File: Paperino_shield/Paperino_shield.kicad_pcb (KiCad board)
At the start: 2 copper layers, 67.3 x 36.9 mm, 6 parts, among them M1 Mounting_hole, M2 Mounting_hole, M3 Mounting_hole, M4 Mounting_hole

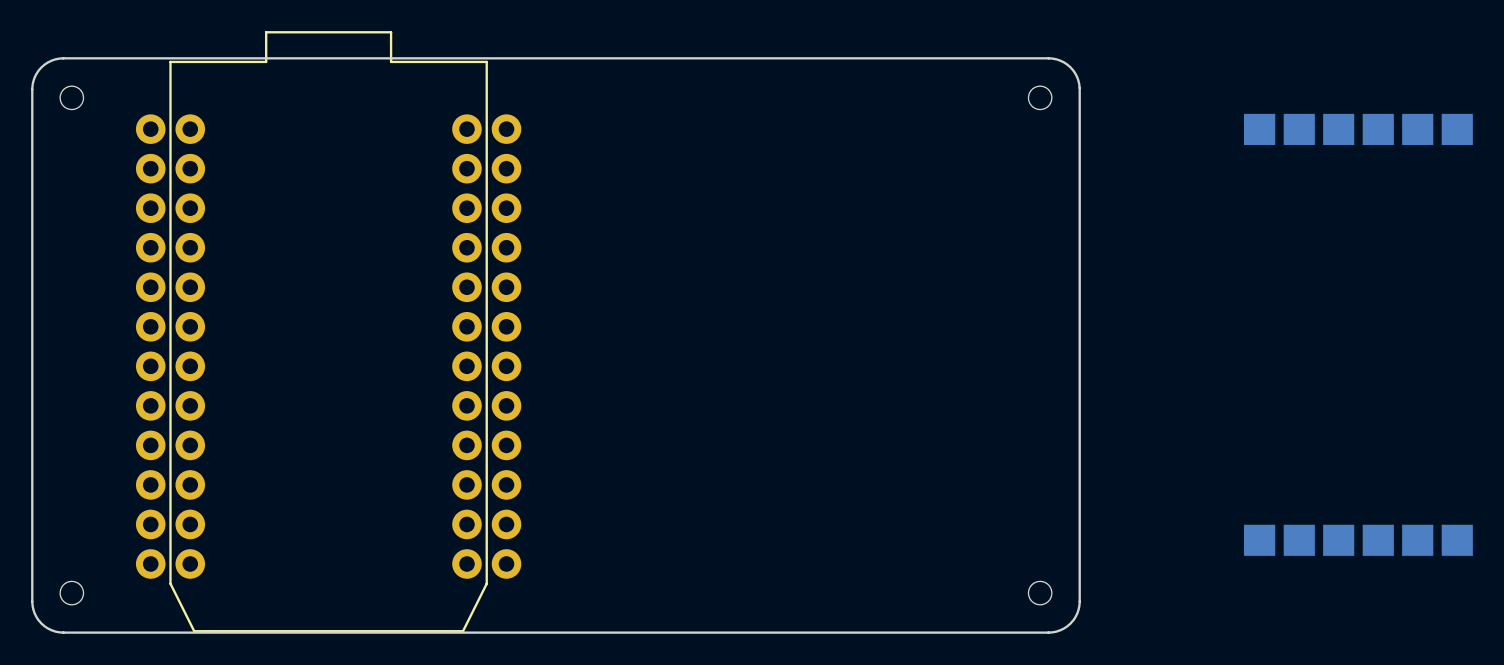
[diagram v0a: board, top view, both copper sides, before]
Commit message: shield mechanical layers
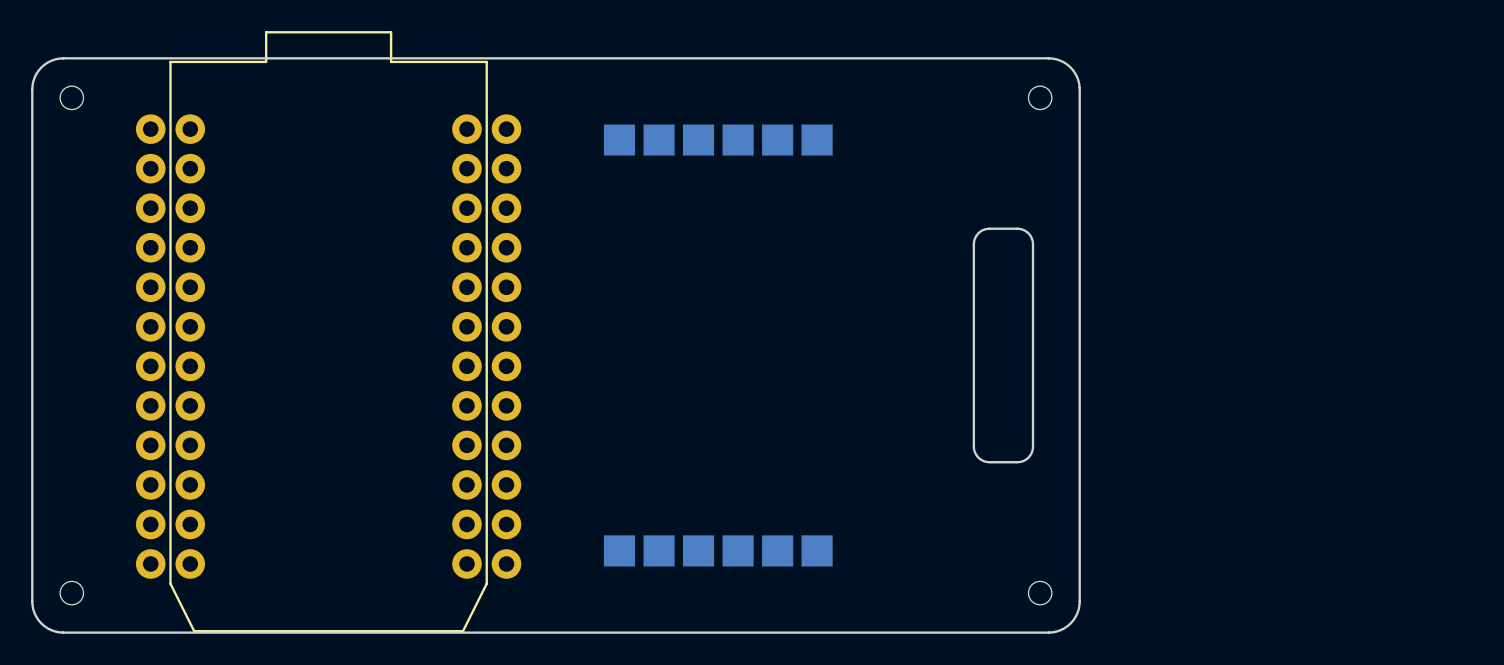
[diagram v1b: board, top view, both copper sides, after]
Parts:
- moved A2 41.1 mm to (147.0, 81.5)
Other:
- outline, holes or cut-outs redrawn
- board text added: "z-axis milling top side -0.8 mm"
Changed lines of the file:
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@@
     (area 99.924999 63.024999 167.375001 100.075001)
     (thickness 1.6)
-    (drawings 8)
+    (drawings 29)
     (tracks 0)
     (zones 0)
@@
     (zone_45_only no)
     (trace_min 0.2)
-    (segment_width 0.2)
+    (segment_width 0.15)
     (edge_width 0.15)
     (via_size 0.6)
@@
     (aux_axis_origin 0 0)
     (grid_origin 100 100)
-    (visible_elements FFFFFF7F)
+    (visible_elements 7FFFFFFF)
     (pcbplotparams
       (layerselection 0x00030_80000001)
@@
       (net 23 +3V3))
   )
-  (module Paperino:paperino_module (layer B.Cu)
-    (at 188.16 80.87 90)
+  (module Paperino:paperino_module locked (layer B.Cu)
+    (at 147.03 81.55 90)
     (fp_text reference A2 (at -11.1 12.35 90) (layer B.SilkS) hide
       (effects (font (size 1 1) (thickness 0.15)) (justify mirror))
@@
     (pad "" np_thru_hole circle (at 0 0) (size 1.5 1.5) (drill 1.5) (layers *.Cu *.Mask))
   )
+  (gr_text "z-axis milling\ntop side\n-0.8 mm" (at 146.91 81.89) (layer Eco1.User)
+    (effects (font (size 1.5 1.5) (thickness 0.3)))
+  )
+  (gr_line (start 132.7 67.27) (end 132.7 95.83) (layer Eco1.User) (width 0.15))
+  (gr_arc (start 133.7 67.27) (end 132.7 67.27) (angle 90) (layer Eco1.User) (width 0.15))
+  (gr_line (start 155.22 66.27) (end 133.7 66.27) (layer Eco1.User) (width 0.15))
+  (gr_arc (start 155.22 67.27) (end 155.22 66.27) (angle 90) (layer Eco1.User) (width 0.15))
+  (gr_line (start 156.22 74.05) (end 156.22 67.27) (layer Eco1.User) (width 0.15))
+  (gr_line (start 162 74.05) (end 156.22 74.05) (layer Eco1.User) (width 0.15))
+  (gr_arc (start 133.7 95.83) (end 133.7 96.83) (angle 90) (layer Eco1.User) (width 0.15))
+  (gr_line (start 155.22 96.83) (end 133.7 96.83) (layer Eco1.User) (width 0.15))
+  (gr_arc (start 155.22 95.83) (end 156.22 95.83) (angle 90) (layer Eco1.User) (width 0.15))
+  (gr_line (start 156.22 89.05) (end 156.22 95.83) (layer Eco1.User) (width 0.15))
+  (gr_line (start 162 89.05) (end 156.22 89.05) (layer Eco1.User) (width 0.15))
+  (gr_line (start 162 89.05) (end 162 74.05) (layer Eco1.User) (width 0.15))
+  (gr_arc (start 161.5 75.05) (end 161.5 74.05) (angle -90) (layer Edge.Cuts) (width 0.15))
+  (gr_line (start 160.5 75.05) (end 160.5 88.05) (layer Edge.Cuts) (width 0.15))
+  (gr_arc (start 161.5 88.05) (end 161.5 89.05) (angle 90) (layer Edge.Cuts) (width 0.15))
+  (gr_line (start 163.3 89.05) (end 161.5 89.05) (layer Edge.Cuts) (width 0.15))
+  (gr_line (start 163.3 74.05) (end 161.5 74.05) (layer Edge.Cuts) (width 0.15))
+  (gr_arc (start 163.3 75.05) (end 163.3 74.05) (angle 90) (layer Edge.Cuts) (width 0.15))
+  (gr_arc (start 163.3 88.05) (end 164.3 88.05) (angle 90) (layer Edge.Cuts) (width 0.15))
+  (gr_line (start 164.3 75.05) (end 164.3 88.05) (layer Edge.Cuts) (width 0.15))
   (gr_arc (start 165.3 65.1) (end 165.3 63.1) (angle 87.13759477) (layer Edge.Cuts) (width 0.15))
   (gr_arc (start 165.3 98) (end 167.3 98) (angle 90) (layer Edge.Cuts) (width 0.15))

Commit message: shield: preliminary layout done
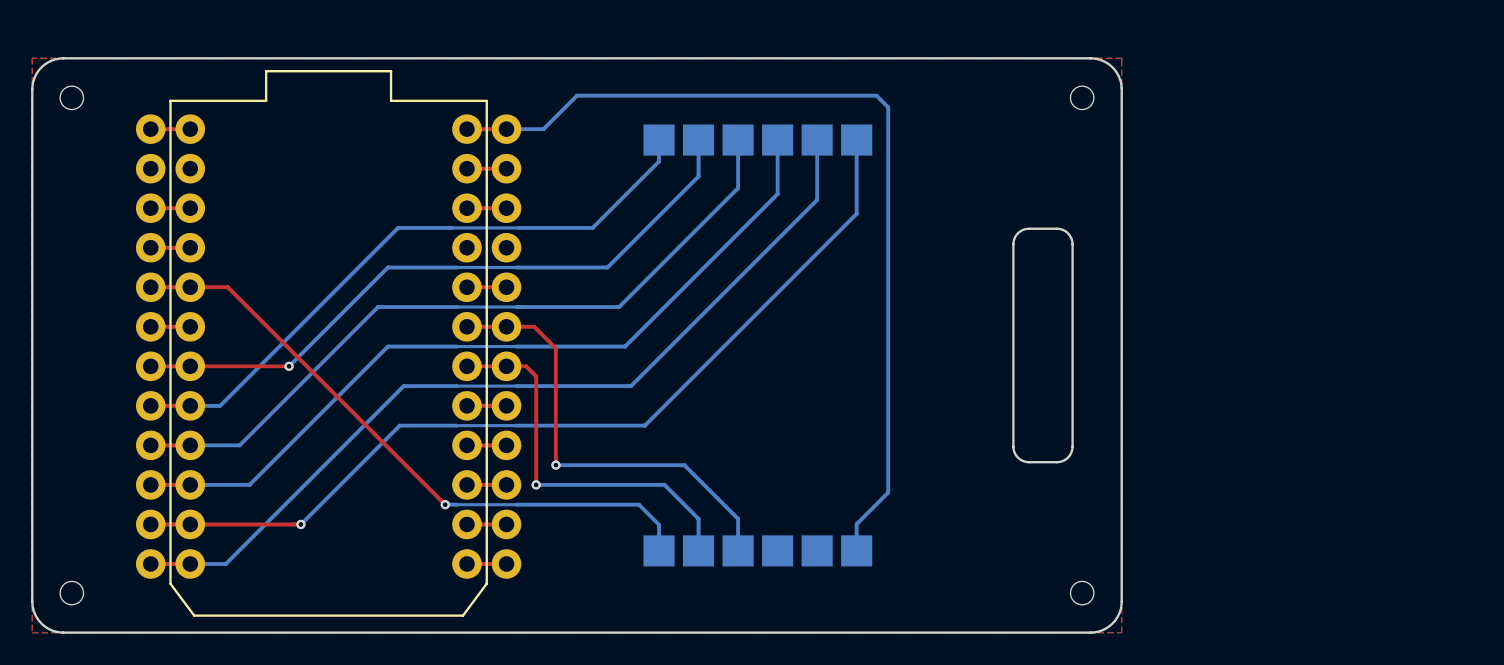
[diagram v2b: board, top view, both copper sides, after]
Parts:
- moved M2 2.70 mm to (167.5, 65.6)
- moved M4 2.70 mm to (167.5, 97.5)
- moved A2 2.54 mm to (149.6, 81.5)
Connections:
- A1 pad 18: Net-(A1-Pad18) -> /INT2
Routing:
- net /~BUSY: track 0.00 -> 57.9 mm, vias 0 -> 1
- net +3V3: track 0.00 -> 57.1 mm
- net /~RST: track 0.00 -> 55.9 mm
- net /SPI_CS1: track 0.00 -> 51.0 mm
- net /SPI_CLK: track 0.00 -> 47.4 mm
- net /SPI_MOSI: track 0.00 -> 42.1 mm, vias 0 -> 1
- net /INT1: track 0.00 -> 40.2 mm, vias 0 -> 1
- net /SPI_MISO: track 0.00 -> 40.0 mm
- net /SPI_CS2: track 0.00 -> 28.5 mm, vias 0 -> 1
- net /INT2: track 0.00 -> 24.6 mm, vias 0 -> 1
- net Net-(A1-Pad6): track 0.00 -> 2.54 mm
- net Net-(A1-Pad4): track 0.00 -> 2.54 mm
- net Net-(A1-Pad3): track 0.00 -> 2.54 mm
- net Net-(A1-Pad1): track 0.00 -> 2.54 mm
- net Net-(A1-Pad23): track 0.00 -> 2.54 mm
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- added copper zone on B.Cu, net GND
- added copper zone on F.Cu, net GND
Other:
- board size 67.3 x 36.9 mm -> 70 x 36.9 mm
- net class Default: via_drill 0.4 -> 0.3

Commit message: silkscreen change
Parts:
- added REF***: OSHW-Symbol_6.7x6mm_SilkScreen, Symbols:OSHW-Symbol_6.7x6mm_SilkScreen, B.Cu at (118.8, 93.0)
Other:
- board text added: "Paperino shield for Particle Photon/ Electron bluz.io licensed under CC-BY 4.0"
- board text added: "USB"
